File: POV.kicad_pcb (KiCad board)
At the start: 2 copper layers, 69.5 x 23.5 mm, 14 parts, among them IC1 ATTINY85-P, SW1 SPDT

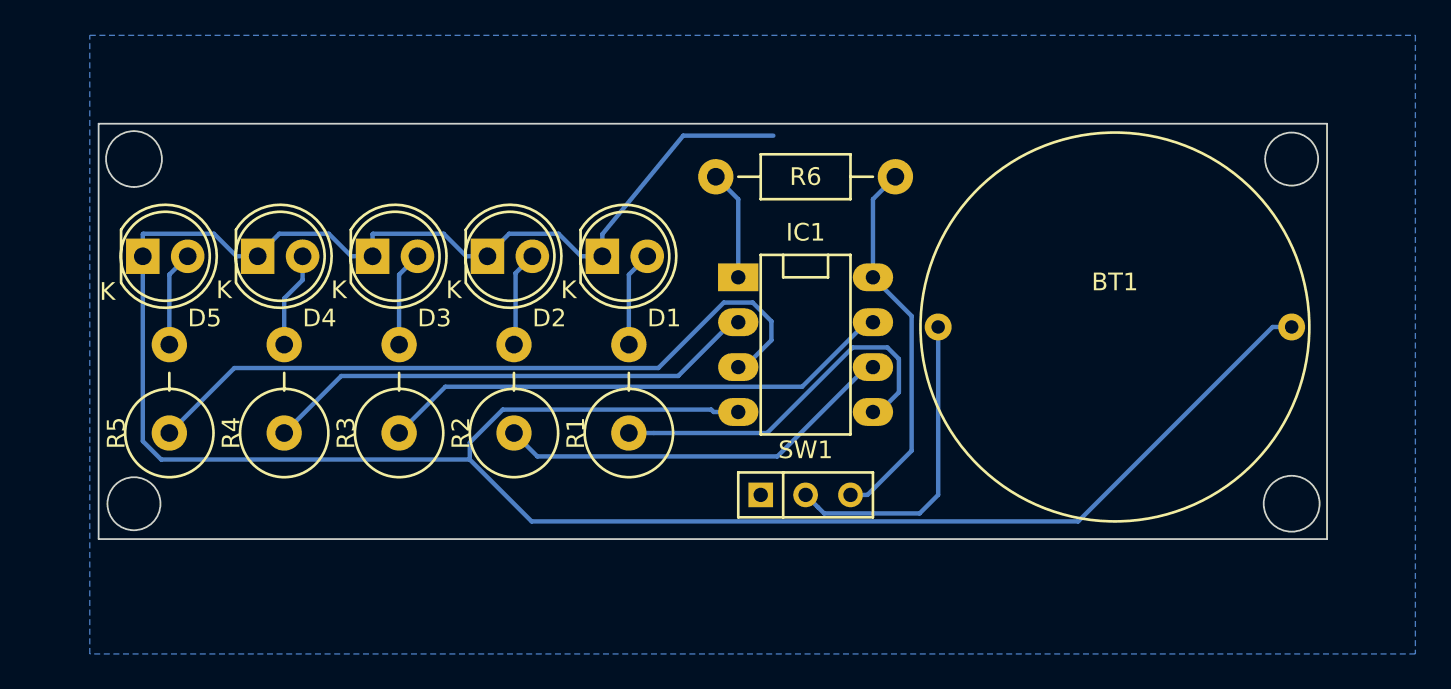
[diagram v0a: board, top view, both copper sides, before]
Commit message: Added gerbers, updated FP,added logos
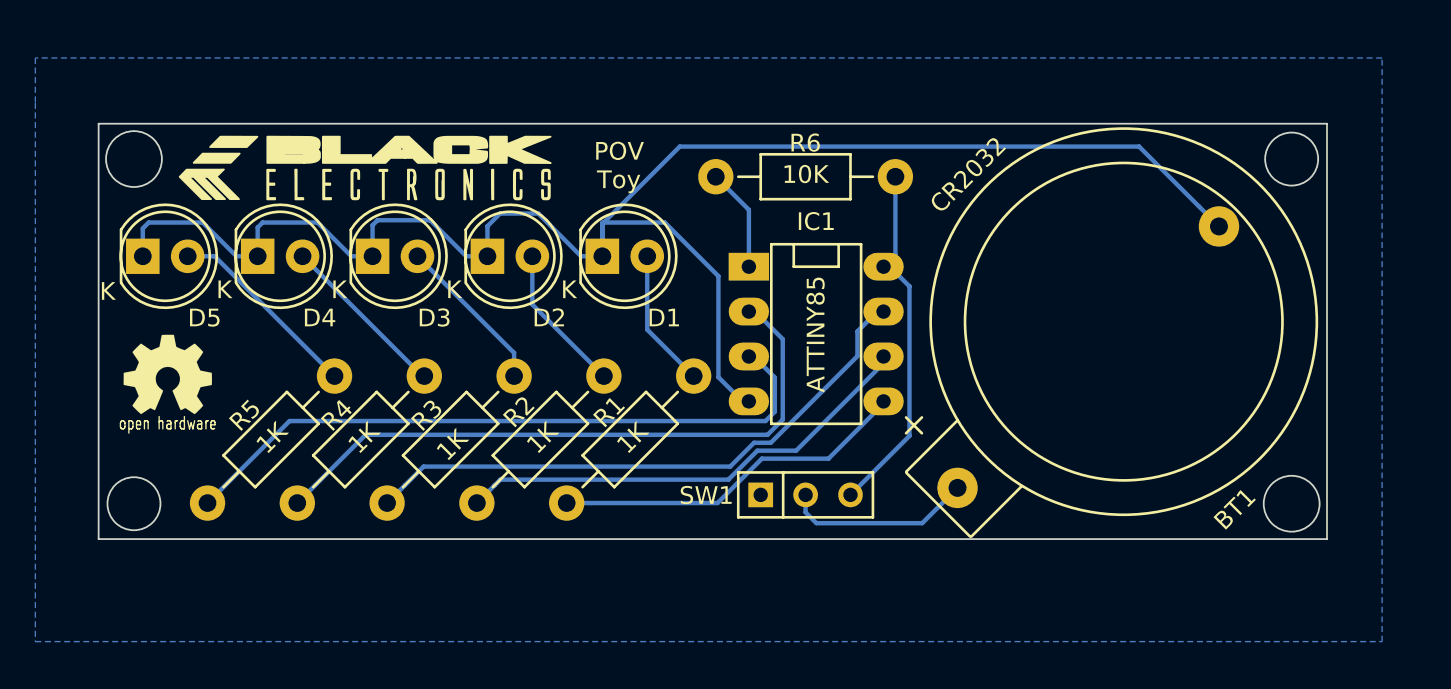
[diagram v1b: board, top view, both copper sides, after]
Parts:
- added P1: Logo, logo:3k5, F.Cu at (140.6, 87.5)
- added P2: openHW, logo:oshw-logo-kicad-copper-10mm, F.Cu at (129.4, 99.2)
- BT1: footprint terminal:CR2032 -> terminal:CR2032H
- IC1: value ATTINY85-P -> ATTINY85
- R1, R2, R3, R4, R5: footprint Resistors_ThroughHole:Resistor_Vertical_RM5mm -> Resistors_ThroughHole:Resistor_Horizontal_RM10mm
- moved R5 6.43 mm to (135.3, 102.9), turned to 45 degrees
- moved R4 5.20 mm to (140.3, 102.9), turned to 45 degrees
- moved R3 4.09 mm to (145.4, 102.9), turned to 45 degrees
- moved R2 3.24 mm to (150.5, 102.9), turned to 45 degrees
- moved R1 2.87 mm to (155.6, 102.9), turned to 45 degrees
- moved IC1 0.85 mm to (166.1, 96.9)
- moved BT1 0.58 mm to (183.5, 96.2), turned to 225 degrees
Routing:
- net GND: track 144.2 -> 94.9 mm
- net Net-(IC1-Pad2): track 28.3 -> 36.5 mm
- net Net-(BT1-Pad1): track 17.9 -> 10.7 mm
- net /D4: track 5.43 -> 11.1 mm
- net /MISO: track 23.0 -> 27.9 mm
- net /D3: track 5.43 -> 9.69 mm
- net /SCK: track 29.4 -> 33.4 mm
- net /D2: track 5.43 -> 9.04 mm
- net /D1: track 5.43 -> 8.45 mm
- net Net-(IC1-Pad3): track 41.1 -> 38.5 mm
- net /D0: track 5.43 -> 7.87 mm
- net /MOSI: track 22.5 -> 20.6 mm
- net /3V3: track 21.4 -> 20.5 mm
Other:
- board text added: "POV Toy"
